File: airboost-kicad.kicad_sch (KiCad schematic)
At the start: 8 parts, among them SW1 SW_Push "Mute", SW2 SW_Push "Next", U1 Display OLED, U2 SCD30

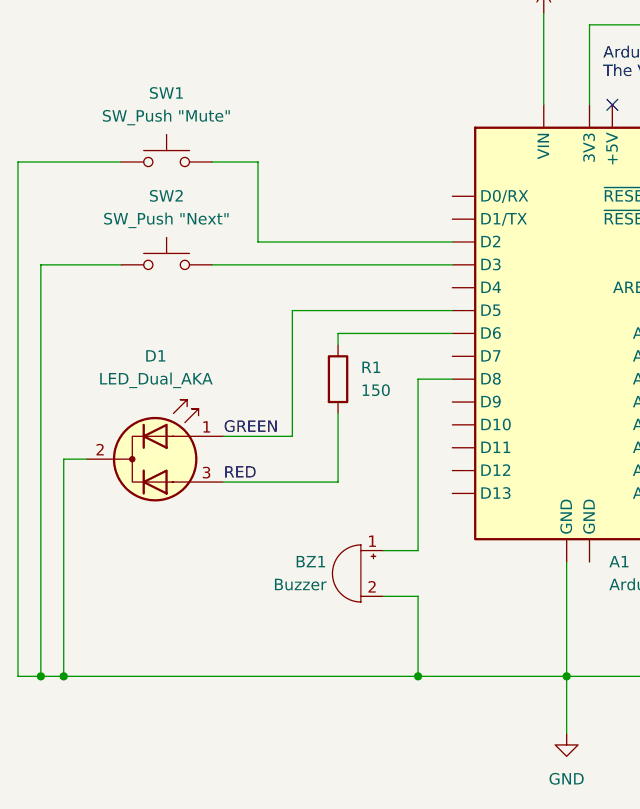
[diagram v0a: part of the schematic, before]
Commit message: fix: reposition resistor for bicolor led
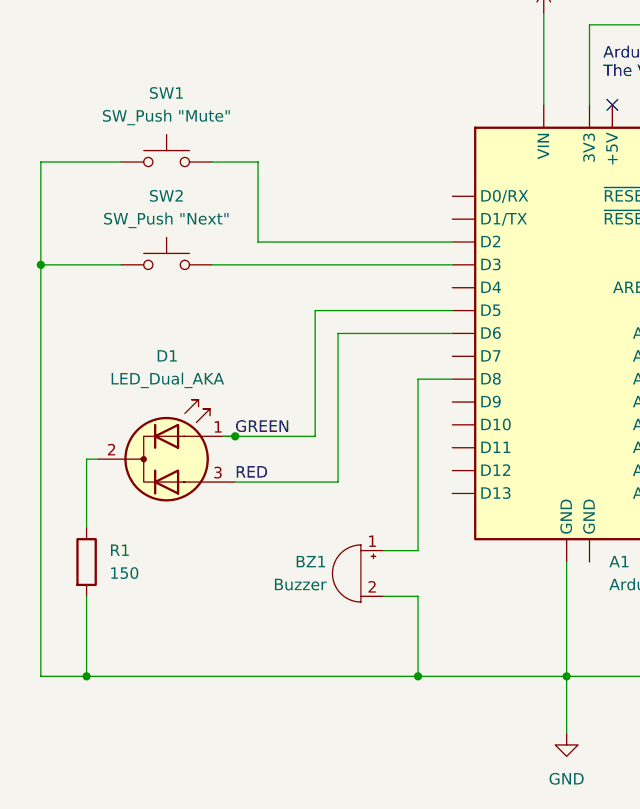
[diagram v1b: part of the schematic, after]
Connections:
- net GND: now also R1.2; no longer D1.2 (K)
- net RED: now also A1.9 (D6); no longer R1.2
- net at R1.1: now also D1.2 (K); no longer A1.9 (D6)
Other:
- moved on the sheet: D1
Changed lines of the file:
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@@
 		(title "Airboost")
 		(date "2024-05-26")
-		(rev "v1.0.0")
+		(rev "v1.0.1")
 	)
 	(junction
@@
 	)
 	(junction
-		(at 27.94 96.52)
+		(at 30.48 96.52)
 		(diameter 0)
 		(color 0 0 0 0)
@@
 	)
 	(junction
+		(at 25.4 50.8)
+		(diameter 0)
+		(color 0 0 0 0)
+	)
+	(junction
 		(at 172.72 35.56)
 		(diameter 0)
@@
 	)
 	(junction
-		(at 25.4 96.52)
+		(at 46.99 69.85)
 		(diameter 0)
 		(color 0 0 0 0)
@@
 	(wire
 		(pts
-			(xy 27.94 72.39) (xy 27.94 96.52)
-		)
-		(stroke
-			(width 0)
-			(type default)
-		)
-	)
-	(wire
-		(pts
-			(xy 53.34 55.88) (xy 53.34 69.85)
-		)
-		(stroke
-			(width 0)
-			(type default)
-		)
-	)
-	(wire
-		(pts
-			(xy 22.86 39.37) (xy 22.86 96.52)
+			(xy 30.48 72.39) (xy 30.48 80.01)
+		)
+		(stroke
+			(width 0)
+			(type default)
+		)
+	)
+	(wire
+		(pts
+			(xy 30.48 87.63) (xy 30.48 96.52)
+		)
+		(stroke
+			(width 0)
+			(type default)
+		)
+	)
+	(wire
+		(pts
+			(xy 55.88 55.88) (xy 55.88 69.85)
+		)
+		(stroke
+			(width 0)
+			(type default)
+		)
+	)
+	(wire
+		(pts
+			(xy 25.4 39.37) (xy 25.4 50.8)
 		)
 		(stroke
@@
 	(wire
 		(pts
-			(xy 27.94 96.52) (xy 67.31 96.52)
-		)
-		(stroke
-			(width 0)
-			(type default)
-		)
-	)
-	(wire
-		(pts
 			(xy 123.19 48.26) (xy 137.16 48.26)
 		)
@@
 	(wire
 		(pts
-			(xy 58.42 67.31) (xy 58.42 74.93)
+			(xy 58.42 58.42) (xy 58.42 74.93)
 		)
 		(stroke
@@
 	(wire
 		(pts
-			(xy 34.29 39.37) (xy 22.86 39.37)
+			(xy 34.29 39.37) (xy 25.4 39.37)
 		)
 		(stroke
@@
 	(wire
 		(pts
+			(xy 25.4 50.8) (xy 25.4 96.52)
+		)
+		(stroke
+			(width 0)
+			(type default)
+		)
+	)
+	(wire
+		(pts
 			(xy 123.19 83.82) (xy 140.97 83.82)
 		)
@@
 	(wire
 		(pts
-			(xy 58.42 74.93) (xy 45.72 74.93)
+			(xy 58.42 74.93) (xy 46.99 74.93)
 		)
 		(stroke
@@
 	(wire
 		(pts
-			(xy 22.86 96.52) (xy 25.4 96.52)
-		)
-		(stroke
-			(width 0)
-			(type default)
-		)
-	)
-	(wire
-		(pts
 			(xy 168.91 53.34) (xy 167.64 53.34)
 		)
@@
 	(wire
 		(pts
-			(xy 27.94 72.39) (xy 30.48 72.39)
+			(xy 30.48 72.39) (xy 31.75 72.39)
 		)
 		(stroke
@@
 		)
 	)
-	(wire
-		(pts
-			(xy 25.4 50.8) (xy 25.4 96.52)
-		)
-		(stroke
-			(width 0)
-			(type default)
-		)
-	)
-	(wire
-		(pts
-			(xy 58.42 58.42) (xy 58.42 59.69)
-		)
-		(stroke
-			(width 0)
-			(type default)
-		)
-	)
 	(bus
 		(pts
@@
 	(wire
 		(pts
-			(xy 53.34 55.88) (xy 71.12 55.88)
-		)
-		(stroke
-			(width 0)
-			(type default)
-		)
-	)
-	(wire
-		(pts
-			(xy 25.4 96.52) (xy 27.94 96.52)
+			(xy 55.88 55.88) (xy 71.12 55.88)
+		)
+		(stroke
+			(width 0)
+			(type default)
+		)
+	)
+	(wire
+		(pts
+			(xy 25.4 96.52) (xy 30.48 96.52)
+		)
+		(stroke
+			(width 0)
+			(type default)
+		)
+	)
+	(wire
+		(pts
+			(xy 30.48 96.52) (xy 67.31 96.52)
 		)
 		(stroke
@@
 	(wire
 		(pts
-			(xy 45.72 69.85) (xy 53.34 69.85)
+			(xy 46.99 69.85) (xy 55.88 69.85)
 		)
 		(stroke
@@
 		(pts
 			(xy 172.72 35.56) (xy 172.72 24.13)
+		)
+		(stroke
+			(width 0)
+			(type default)
+		)
+	)
+	(wire
+		(pts
+			(xy 46.99 69.85) (xy 45.72 69.85)
 		)
 		(stroke
@@
 	)
 	(label "RED"
-		(at 45.72 74.93 0)
+		(at 46.99 74.93 0)
 		(fields_autoplaced yes)
 		(effects
@@
 	)
 	(label "GREEN"
-		(at 45.72 69.85 0)
+		(at 46.99 69.85 0)
 		(fields_autoplaced yes)
 		(effects
@@
 				(path "/8083be59-9f45-42ae-bb9c-d5ee5d95f647"
 					(reference "SW2")
+					(unit 1)
+				)
+			)
+		)
+	)
+	(symbol
+		(lib_id "Device:R")
+		(at 30.48 83.82 0)
+		(unit 1)
+		(exclude_from_sim no)
+		(in_bom yes)
+		(on_board yes)
+		(dnp no)
+		(fields_autoplaced yes)
+		(property "Reference" "R1"
+			(at 33.02 82.5499 0)
+			(effects
+				(font
+					(size 1.27 1.27)
+				)
+				(justify left)
+			)
+		)
+		(property "Value" "150"
+			(at 33.02 85.0899 0)
+			(effects
+				(font
+					(size 1.27 1.27)
+				)
+				(justify left)
+			)
+		)
+		(property "Footprint" ""
+			(at 28.702 83.82 90)
+			(effects
+				(font
+					(size 1.27 1.27)
+				)
+				(hide yes)
+			)
+		)
+		(property "Datasheet" "~"
+			(at 30.48 83.82 0)
+			(effects
+				(font
+					(size 1.27 1.27)
+				)
+				(hide yes)
+			)
+		)
+		(property "Description" "Resistor"
+			(at 30.48 83.82 0)
+			(effects
+				(font
+					(size 1.27 1.27)
+				)
+				(hide yes)
+			)
+		)
+		(pin "2"
+		)
+		(pin "1"
+		)
+		(instances
+			(project "airboost-kicad"
+				(path "/8083be59-9f45-42ae-bb9c-d5ee5d95f647"
+					(reference "R1")
 					(unit 1)
 				)
@@
 	(symbol
 		(lib_id "Device:LED_Dual_AKA")
-		(at 38.1 72.39 0)
+		(at 39.37 72.39 0)
 		(unit 1)
 		(exclude_from_sim no)
@@
 		(fields_autoplaced yes)
 		(property "Reference" "D1"
-			(at 38.1635 60.96 0)
+			(at 39.4335 60.96 0)
 			(effects
 				(font
@@
 		)
 		(property "Value" "LED_Dual_AKA"
-			(at 38.1635 63.5 0)
+			(at 39.4335 63.5 0)
 			(effects
 				(font
@@
 		)
 		(property "Footprint" ""
-			(at 38.1 72.39 0)
+			(at 39.37 72.39 0)
 			(effects
 				(font
@@
 		)
 		(property "Datasheet" "~"
-			(at 38.1 72.39 0)
+			(at 39.37 72.39 0)
 			(effects
 				(font
@@
 		)
 		(property "Description" "Dual LED, common cathode on pin 2"
-			(at 38.1 72.39 0)
+			(at 39.37 72.39 0)
 			(effects
 				(font
@@
 					(unit 1)
 				)
-			)
-		)
-	)
-	(symbol
-		(lib_id "Device:R")
-		(at 58.42 63.5 0)
-		(unit 1)
-		(exclude_from_sim no)
-		(in_bom yes)
-		(on_board yes)
-		(dnp no)
-		(fields_autoplaced yes)
-		(property "Reference" "R1"
-			(at 60.96 62.2299 0)
-			(effects
-				(font
-					(size 1.27 1.27)
-				)
-				(justify left)
-			)
-		)
-		(property "Value" "150"
-			(at 60.96 64.7699 0)
-			(effects
-				(font
-					(size 1.27 1.27)
-				)
-				(justify left)
-			)
-		)
-		(property "Footprint" ""
-			(at 56.642 63.5 90)
-			(effects
-				(font
-					(size 1.27 1.27)
-				)
-				(hide yes)
-			)
-		)
-		(property "Datasheet" "~"
-			(at 58.42 63.5 0)
-			(effects
-				(font
-					(size 1.27 1.27)
-				)
-				(hide yes)
-			)
-		)
-		(property "Description" "Resistor"
-			(at 58.42 63.5 0)
-			(effects
-				(font
-					(size 1.27 1.27)
-				)
-				(hide yes)
-			)
-		)
-		(pin "2"
-		)
-		(pin "1"
-		)
-		(instances
-			(project "airboost-kicad"
-				(path "/8083be59-9f45-42ae-bb9c-d5ee5d95f647"
-					(reference "R1")
-					(unit 1)
-				)
